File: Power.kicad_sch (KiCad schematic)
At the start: 82 parts, among them J11 8-pin ATX connector, Q1 MMBT2222A, U21 SiRA80DP, U22 TPS25983, U23 AP7361C-33E, U24 MP8795, U25 MIC23201YML-TR

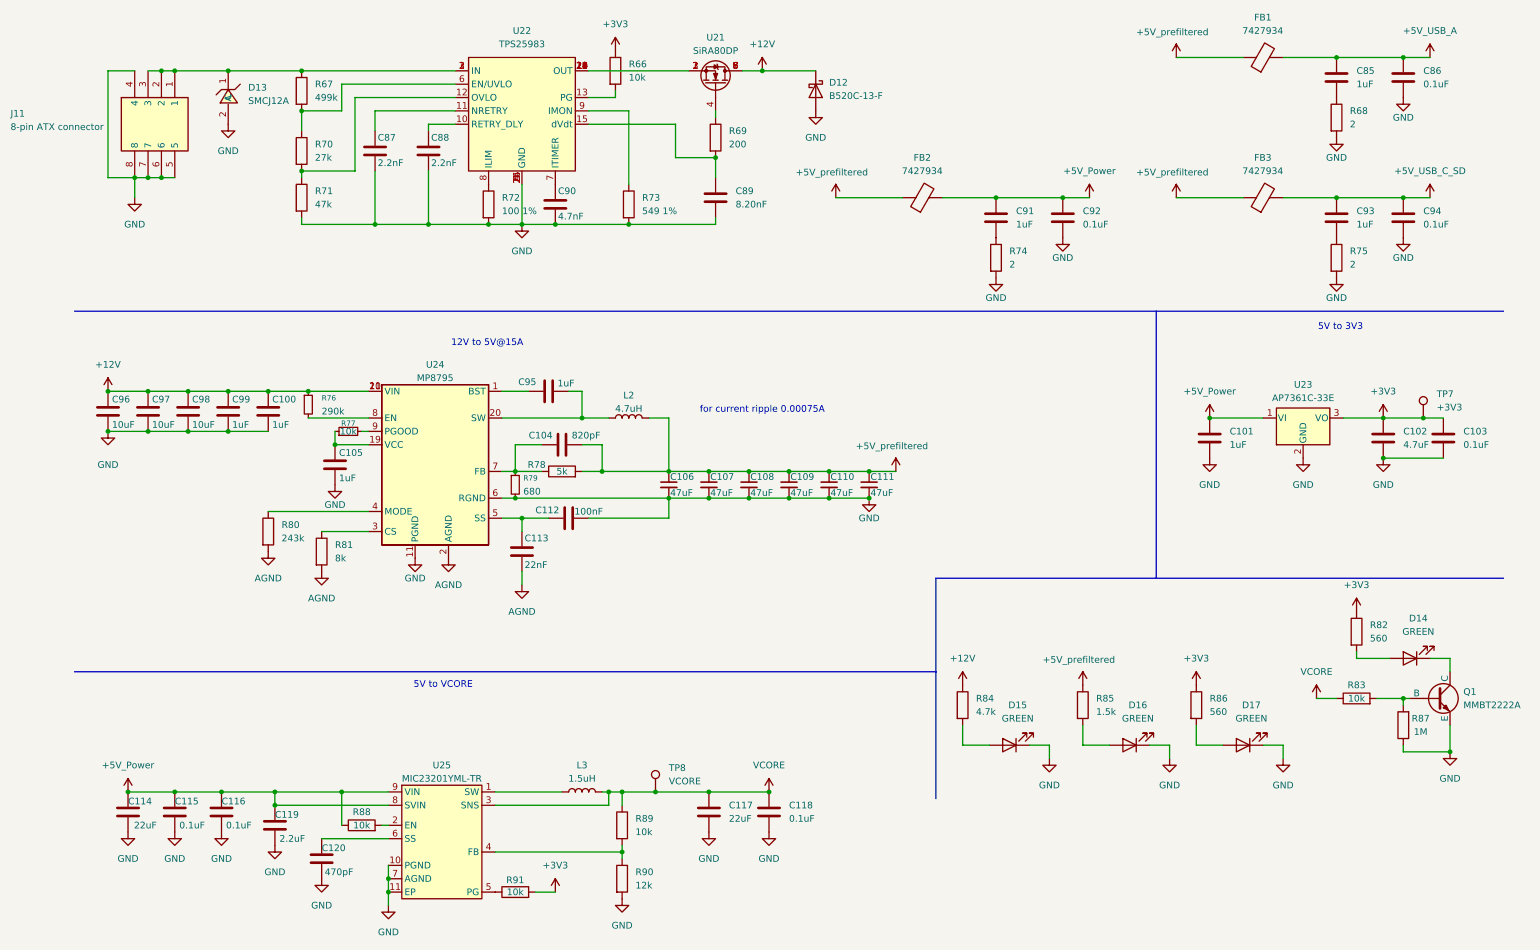
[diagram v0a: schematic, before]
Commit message: Design rule file added, lots of minor tweaks, routing done (including differential pairs), DRC done/
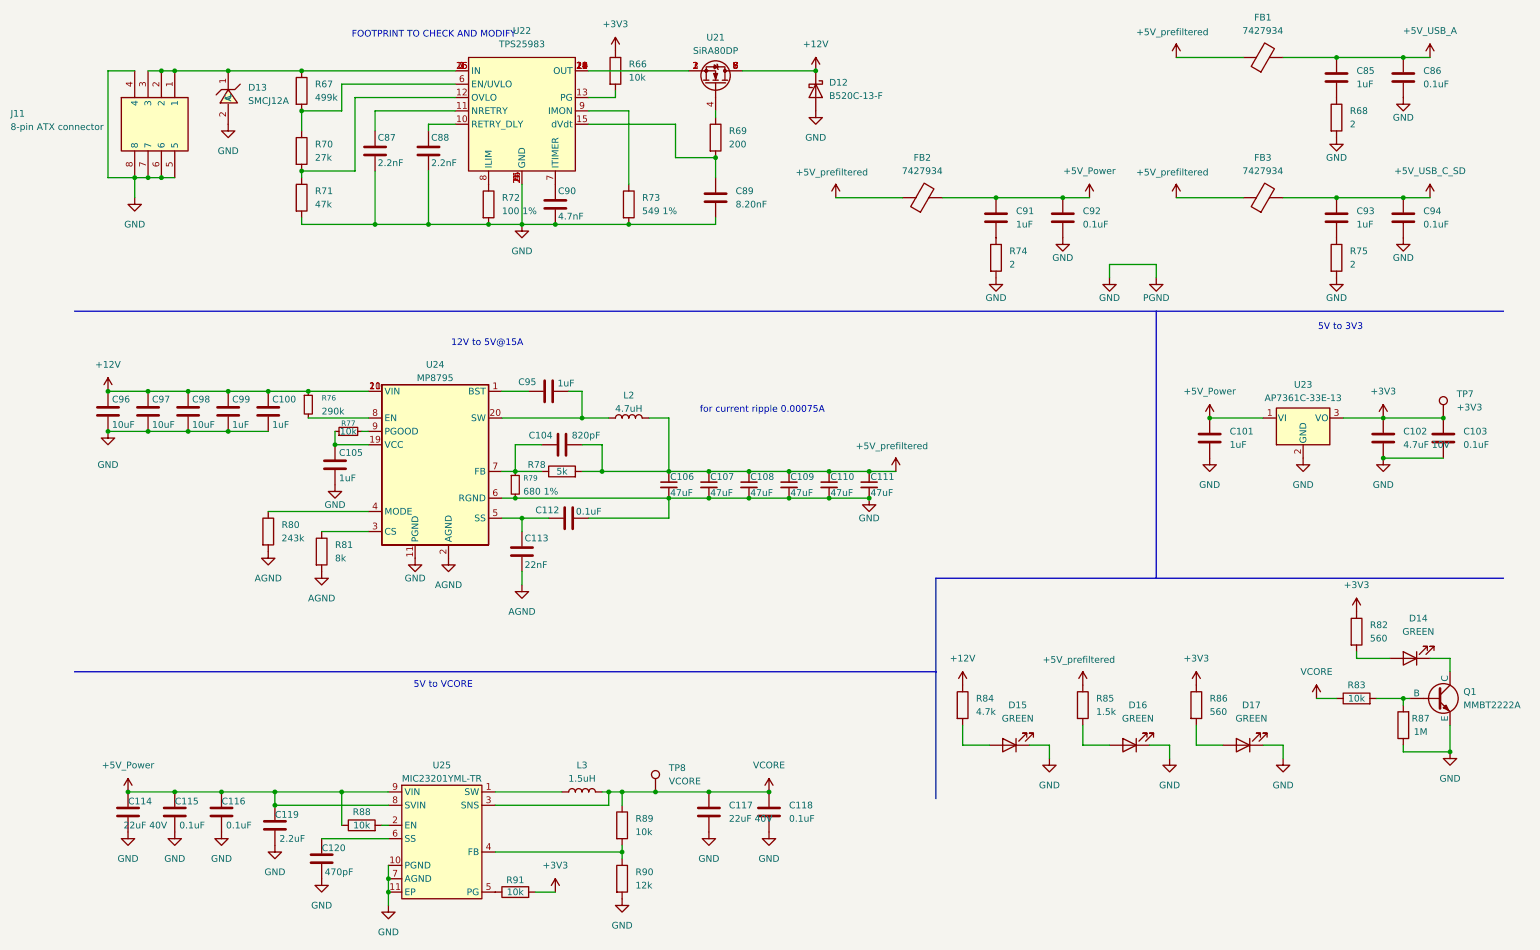
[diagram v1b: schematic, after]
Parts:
- C102: value 4.7uF -> 4.7uF 10V; footprint Capacitor_SMD:C_0805_2012Metric -> Capacitor_SMD:C_0402_1005Metric; LCSC Part C6119944 -> C318563
- C103, C115, C116, C118, C86, C92, C94: LCSC Part C181043 -> C181043
- C112: value 100nF -> 0.1uF; LCSC Part C181043 -> C181043
- C114, C117: value 22uF -> 22uF 40V; footprint Capacitor_SMD:C_1812_4532Metric -> Capacitor_SMD:C_1206_3216Metric; LCSC Part C141660 -> C309062
- FB1, FB2, FB3: LCSC Part C5429469 -> (none); Mouser Part No  710-7427934 -> 710-7427934
- Q1: LCSC Part C82460 -> C82460
- R68, R74, R75: LCSC Part C2907139 -> C2907139
- R69: LCSC Part C114764 -> C114764
- R71: LCSC Part C93943 -> C93943
- R72: LCSC Part C106232 -> C106232
- R76: LCSC Part C5126158 -> C5126158
- R78: LCSC Part C5948099 -> C5948099
- R79: value 680 -> 680 1%; LCSC Part C25130 -> C25130
- R82, R86: LCSC Part C137858 -> C137858
- R85: LCSC Part C327253 -> C327253
- R90: LCSC Part C413006 -> C413006
- TP7, TP8: now left out of the parts list
- U21: Mouser Part No  78-SIRA80DP-T1-RE3 -> (none)
- U22: LCSC Part C20611808 -> C20611808
- U23: value AP7361C-33E -> AP7361C-33E-13
- U24: LCSC Part C3188708 -> (none); Mouser Part No  (none) -> 946-MP8795GLE-Z
- U25: Mouser Part No  998-MIC23201YMLTR -> (none)
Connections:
- net at D13.1 (C), J11.1, J11.2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: now also U22.16 (IN), U22.25 (IN)
- net at U21.1 (S), U21.2 (S), U21.3 (S)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: no longer U22.25 (OUT)
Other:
- note added: "FOOTPRINT TO CHECK AND MODIFY"
- company: (none) -> Karol Woźniak
- moved on the sheet: TP7
